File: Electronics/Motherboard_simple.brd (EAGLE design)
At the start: 83.3 x 49.8 mm, 53 parts, among them IC1 NE556D, IC2 741G3157DBVR, IC3 741G3157DBVR, IC4 TINY25, J1 AVRISP, Q1 2N3904, Q2 2N3904, U2 USD-SOCKETNEW

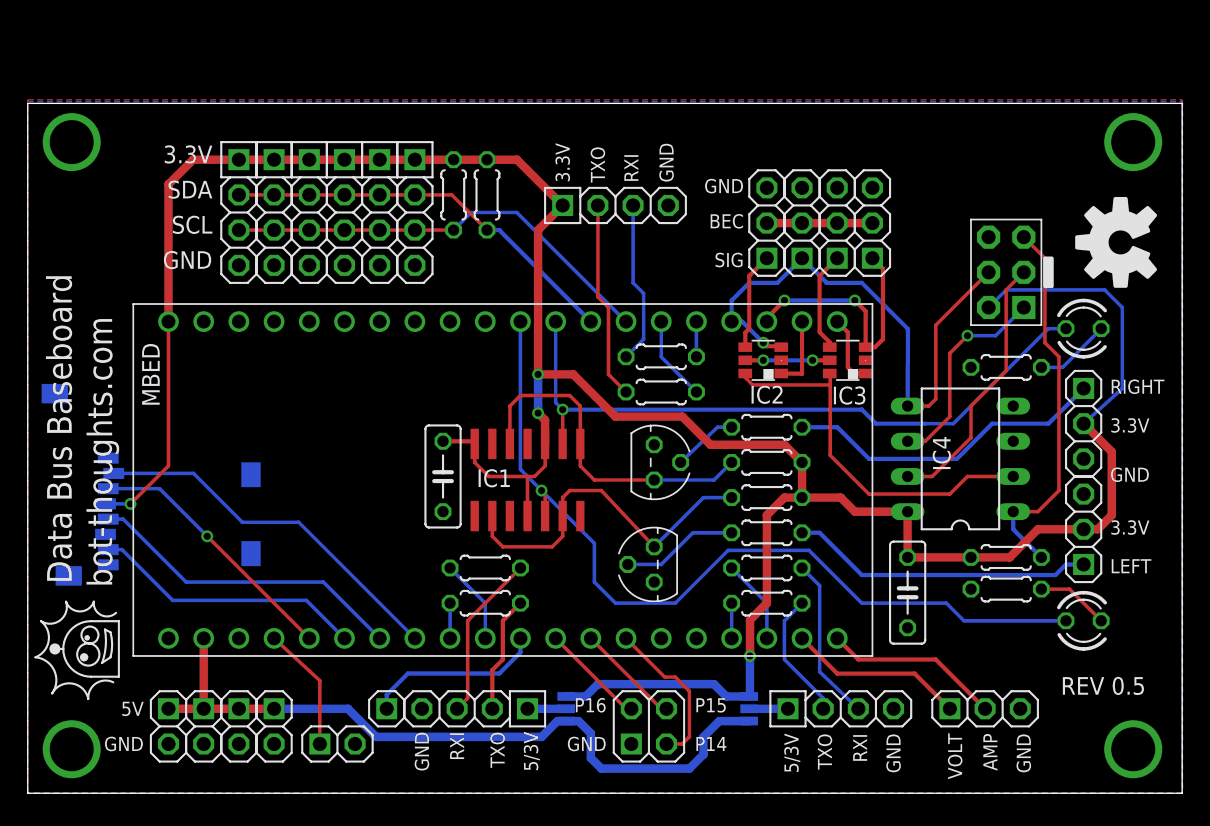
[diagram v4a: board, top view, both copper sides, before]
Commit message: Moved RC Mux to subdirectory. Minor changes to various other boards.
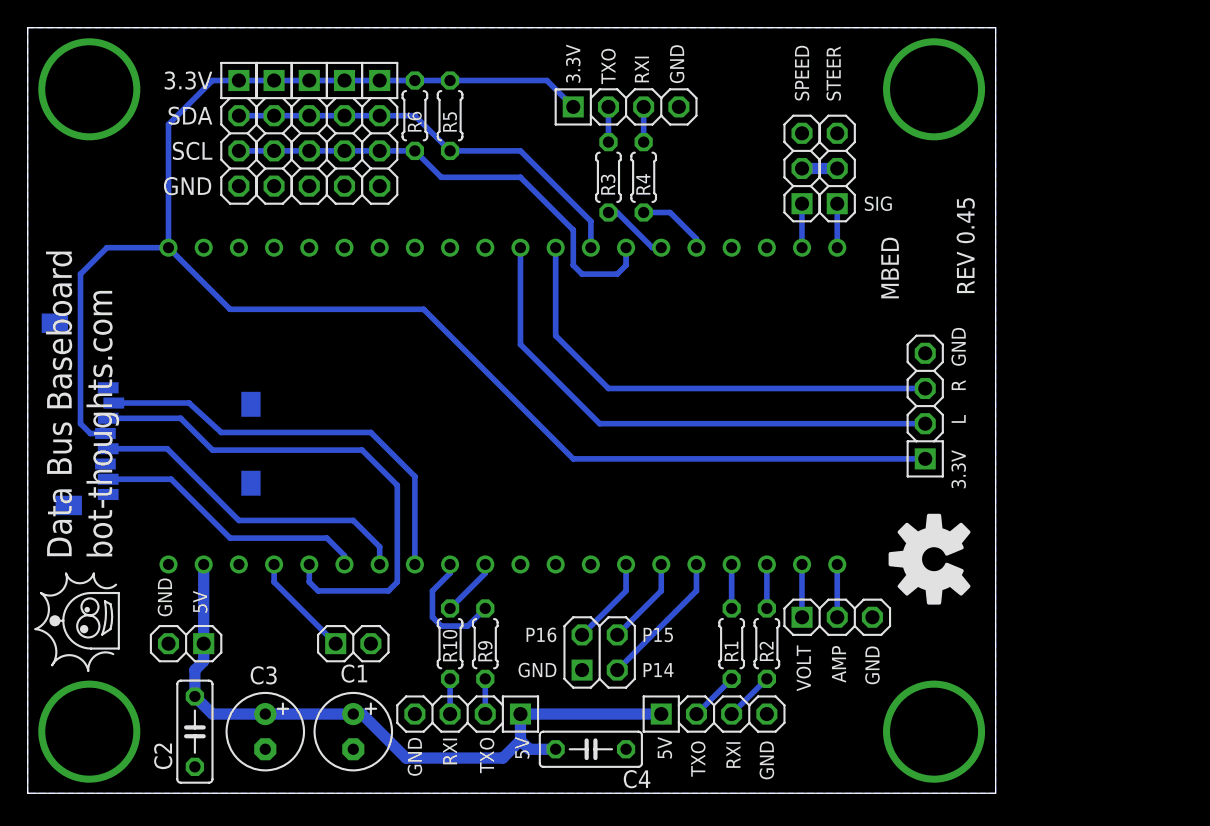
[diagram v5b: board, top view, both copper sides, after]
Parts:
- removed IC1: NE556D, linear:SO14
- removed IC2, IC3: 741G3157DBVR, 74xx-little-us:DBV_R-PDSO-G6
- removed IC4: TINY25, avr-7:DIL08
- removed J1: AVRISP, ads4:CON6P2R
- removed JP16, JP18, JP23: POWER, pinhead-2:1X02-S
- removed JP19: ENCODERS, pinhead-2:1X03-S
- removed JP20: I2C, pinhead-2:1X04-S
- removed JP21: RXE, pinhead-2:1X03-S
- removed JP22: RXS, pinhead-2:1X03-S
- removed JP7: PPS, pinhead-2:1X01-S
- removed LED_L, LED_R: (no value), led:LED3MM
- removed Q1, Q2: 2N3904, mes_transistors:TO92
- removed R11, R12, R15: 10k, rcl:0204/5
- removed R13, R14: 1k, rcl:0204/5
- removed R7, R8: 330, rcl:0204/5
- removed SJ1, SJ2: (no value), SparkFun:SJ_3
- added C3: 10uF, rcl:E2,5-6
- added C4: 0.01uF, rcl:C050-025X075
- C1: value 104 -> 470uF; device rcl:C050-025X075 -> rcl:E2,5-6
- C2: value 104 -> 0.01uF
- JP15: device pinhead-2:1X03-S -> pinhead-2:1X04-S
- JP8: value ESC -> SPEED
- JP9: value SRV -> STEER
- moved C1 41.2 mm to (23.5, 4.45)
- moved C2 25.7 mm to (12.1, 4.45)
- moved R3 16.0 mm to (41.9, 44.5), turned to 90 degrees
- moved JP15 14.5 mm to (64.8, 27.9)
- moved R4 13.0 mm to (44.5, 44.5), turned to 90 degrees
- moved JP17 12.5 mm to (58.4, 12.7)
- moved JP6 9.15 mm to (49.5, 5.71)
- moved JP4 7.33 mm to (23.5, 10.8)
- moved JP2 7.15 mm to (43.2, 49.5)
- moved JP3 7.08 mm to (11.4, 10.8), turned to 180 degrees
- moved JP1 6.41 mm to (41.3, 10.2)
- moved R6 6.36 mm to (27.9, 48.9)
- moved R5 6.31 mm to (30.5, 48.9)
- moved R10 6.02 mm to (30.5, 10.8), turned to 270 degrees
- moved JP11 5.72 mm to (20.3, 47.6)
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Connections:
- removed net !TRST: IC4.1, J1.5, R15.1
- removed net BEC: JP21.2, JP22.2, JP8.2, JP9.2
- removed net ESC: IC2.4, JP8.1
- removed net MCUESC: IC2.1, MBED.P$22
- removed net MCUSRV: IC3.1, MBED.P$21
- removed net MCU_LEFT: IC1.5, LED_L.A, MBED.P$30
- removed net MCU_RIGHT: IC1.9, LED_R.A, MBED.P$29
- removed net MISO: IC4.6, J1.1
- removed net N$11: IC1.12, IC1.8, Q2.1, R12.1
- removed net N$12: IC1.2, IC1.6, Q1.1, R11.1
- removed net N$13: Q2.2, R13.1
- removed net N$14: Q1.2, R14.1
- removed net N$18: JP10.1, SJ1.2
- removed net N$19: JP6.1, SJ2.2
- removed net N$25: IC2.6, IC3.6, IC4.2
- removed net N$4: LED_R.K, R8.2
- removed net PPS: JP7.1, MBED.P$11
- removed net RXESC: IC2.3, IC4.5, J1.4, JP21.1, MBED.P$24
- removed net RXSRV: IC3.3, JP22.1, MBED.P$23
- removed net SCK: IC4.7, J1.3
- removed net SRV: IC3.4, JP9.1
- removed net VCC: IC2.5, IC3.5
- new net SPEED: JP8.1, MBED.P$22
- new net STEER: JP9.1, MBED.P$21
- net +3V3: now also JP15.1; no longer C1.1, C2.1, IC1.10, IC1.14, IC1.4, IC4.8, J1.2, JP15.2, JP19.2, JP20.1, R11.2, R12.2, R15.2, SJ1.3, SJ2.3
- net +5V: now also C1.+, C2.1, C3.+, C4.1, JP10.1, JP6.1; no longer JP16.1, JP18.1, JP23.1, SJ1.1, SJ2.1
- net ENC_LEFT: now also JP15.2, MBED.P$30; no longer JP15.1, R14.2
- net ENC_RIGHT: now also JP15.3, MBED.P$29; no longer JP19.1, R13.2
- net GND: now also C1.-, C3.-, C4.2, JP15.4; no longer C1.2, IC1.7, IC2.2, IC3.2, IC4.4, J1.6, JP15.3, JP16.2, JP18.2, JP19.3, JP20.4, JP21.3, JP22.3, JP23.2, Q1.3, Q2.3, R7.1, R8.1
- net N$3: now also JP8.2, JP9.2; no longer LED_L.K, R7.2
- net N$5: now also JP1.2, MBED.P$14; no longer JP1.4, MBED.P$13
- net N$7: now also JP1.4, MBED.P$15; no longer JP1.2, MBED.P$12
- net N$8: now also MBED.P$16; no longer MBED.P$14
- net SCL: no longer JP20.3
- net SDA: no longer JP20.2
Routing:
- net +3V3: track 198.7 -> 121.2 mm, vias 4 -> 0
- net MCU_LEFT: track 61.3 -> 0.00 mm, vias 1 -> 0
- net MCU_RIGHT: track 48.6 -> 0.00 mm, vias 1 -> 0
- net RXESC: track 40.5 -> 0.00 mm, vias 1 -> 0
- net N$25: track 27.5 -> 0.00 mm
- net !TRST: track 27.4 -> 0.00 mm
- net N$12: track 25.6 -> 0.00 mm
- net N$11: track 24.6 -> 0.00 mm
- net SCK: track 19.2 -> 0.00 mm
- net MOSI1: track 19.0 -> 38.0 mm, vias 1 -> 0
- net RXSRV: track 18.5 -> 0.00 mm, vias 2 -> 0
- net ENC_LEFT: track 21.9 -> 38.6 mm
- net MISO: track 15.1 -> 0.00 mm, vias 1 -> 0
- net PPS: track 12.9 -> 0.00 mm
- net N$9: track 14.3 -> 2.54 mm
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- removed copper zone on layer 1, net GND
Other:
- board size 83.3 x 49.8 mm -> 69.8 x 55.2 mm
- board text added: "L"
- board text added: "R"
- board text added: "REV 0.45"
- board text added: "SPEED"
- board text added: "STEER"
- board text removed: "5/3V"
- board text removed: "BEC"
- board text removed: "LEFT"
- board text removed: "REV 0.5"
- board text removed: "RIGHT"
